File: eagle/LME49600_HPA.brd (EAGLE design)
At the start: 93.7 x 71.1 mm, 43 parts, among them IC1 OPA2134P, IC2 OPA2134P, P1 POLYSWITCH, P2 POLYSWITCH

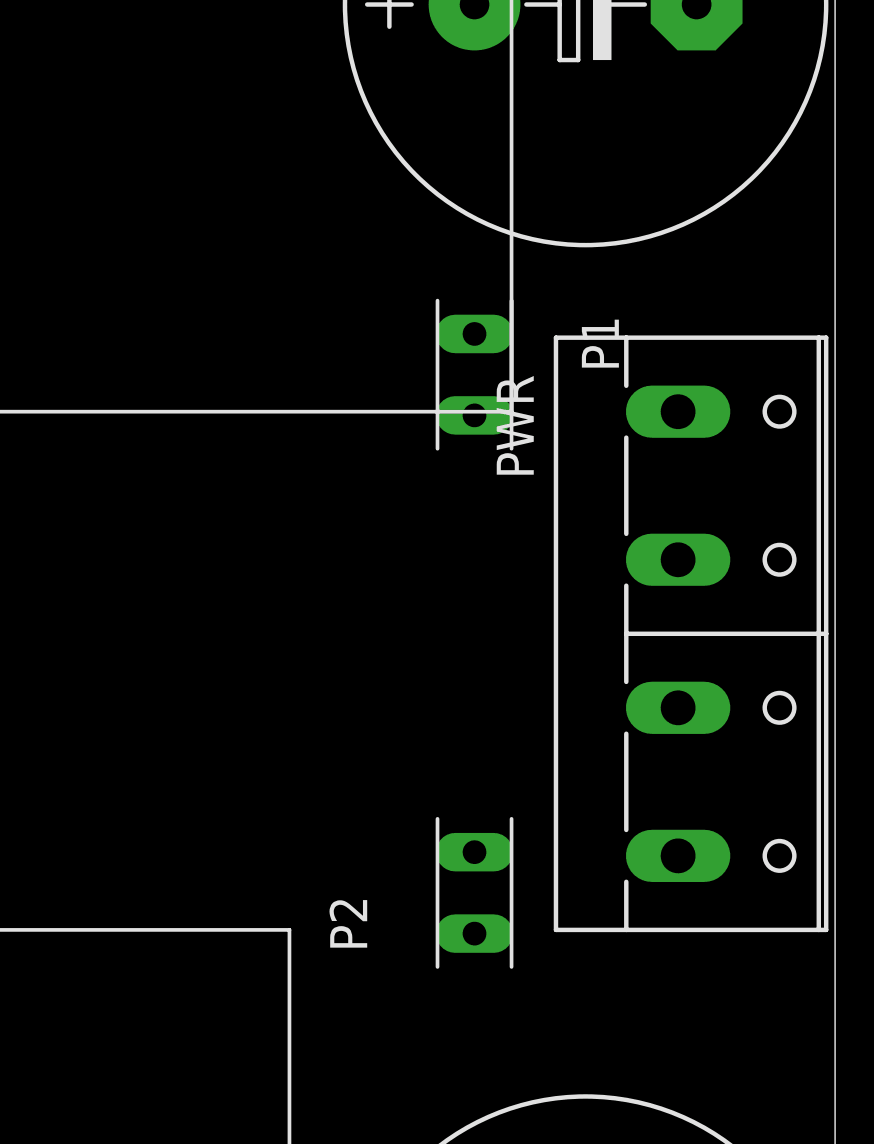
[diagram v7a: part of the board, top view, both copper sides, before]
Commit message: Add: Pilot LED
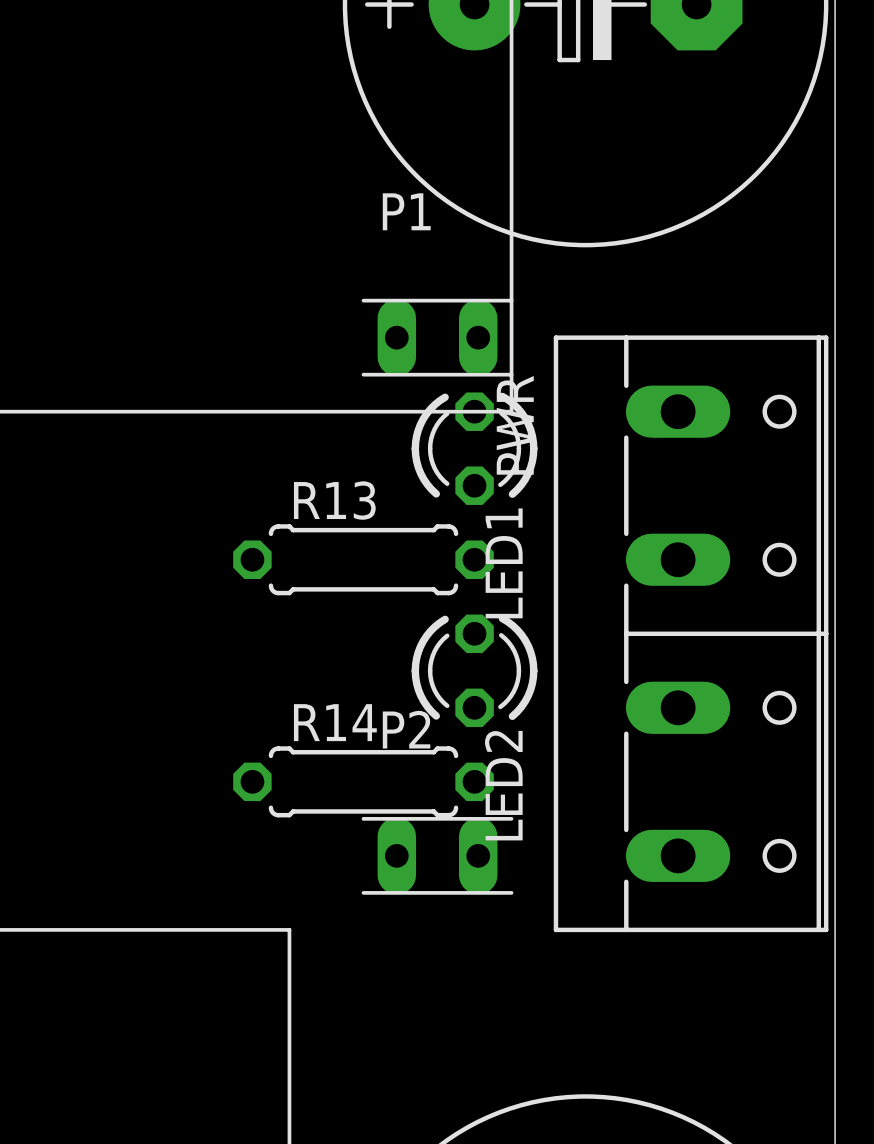
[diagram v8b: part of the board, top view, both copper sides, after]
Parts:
- added LED1: BULE, led:LED3MM
- added LED2: BLUE, led:LED3MM
- added R13, R14: 1k, rcl:0207/7
- moved P2 1.80 mm to (80.0, 30.5), turned to 0 degrees
- moved P1 1.80 mm to (80.0, 48.3), turned to 0 degrees
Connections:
- new net N$17: LED1.K, R13.2
- new net N$19: LED2.K, R14.2
- net AGND: now also LED2.A, R13.1
- net V+: now also LED1.A
- net V-: now also R14.1
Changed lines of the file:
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@@
 <element name="C1" library="rcl" package="E7,5-16" value="470uF" x="85.09" y="59.69"/>
 <element name="C10" library="rcl" package="E7,5-16" value="470uF" x="85.09" y="13.97" rot="R180"/>
-<element name="P1" library="mylib2" package="POLYSWITCH" value="POLYSWITCH" x="81.28" y="46.99" rot="R270"/>
-<element name="P2" library="mylib2" package="POLYSWITCH" value="POLYSWITCH" x="81.28" y="29.21" rot="R90"/>
+<element name="P1" library="mylib2" package="POLYSWITCH" value="POLYSWITCH" x="80.01" y="48.26"/>
+<element name="P2" library="mylib2" package="POLYSWITCH" value="POLYSWITCH" x="80.01" y="30.48"/>
 <element name="C6" library="rcl" package="E2-4" value="4.7uF" x="53.34" y="41.91" rot="R90"/>
 <element name="C7" library="rcl" package="E2-4" value="4.7uF" x="53.34" y="67.31" rot="R270"/>
@@
 <element name="U$1" library="mylib2" package="SIP5-9" value="LME49600-BRD2" x="66.04" y="55.88" rot="R270"/>
 <element name="U$2" library="mylib2" package="SIP5-9" value="LME49600-BRD2" x="58.42" y="17.78" rot="R270"/>
+<element name="LED1" library="led" package="LED3MM" value="BULE" x="81.28" y="44.45" rot="R270"/>
+<element name="LED2" library="led" package="LED3MM" value="BLUE" x="81.28" y="36.83" rot="R270"/>
+<element name="R13" library="rcl" package="0207/7" value="1k" x="77.47" y="40.64"/>
+<element name="R14" library="rcl" package="0207/7" value="1k" x="77.47" y="33.02"/>
 </elements>
 <signals>
@@
 <wire x1="7.62" y1="68.58" x2="35.56" y2="68.58" width="0.4064" layer="16"/>
 <wire x1="5.08" y1="55.88" x2="7.62" y2="53.34" width="0.4064" layer="16"/>
+<contactref element="R13" pad="1"/>
+<contactref element="LED2" pad="A"/>
 <wire x1="88.265" y1="40.64" x2="88.9" y2="59.69" width="0" layer="19" extent="1-1"/>
 <wire x1="88.265" y1="35.56" x2="88.265" y2="40.64" width="0" layer="19" extent="1-1"/>
-<wire x1="88.9" y1="13.97" x2="88.265" y2="35.56" width="0" layer="19" extent="1-1"/>
-<wire x1="53.34" y1="42.926" x2="88.265" y2="40.64" width="0" layer="19" extent="1-1"/>
+<wire x1="81.28" y1="38.1" x2="88.265" y2="40.64" width="0" layer="19" extent="1-1"/>
+<wire x1="73.66" y1="40.64" x2="81.28" y2="38.1" width="0" layer="19" extent="1-1"/>
+<wire x1="53.34" y1="42.926" x2="73.66" y2="40.64" width="0" layer="19" extent="1-1"/>
 <wire x1="43.18" y1="35.56" x2="43.18" y2="38.1" width="0" layer="19" extent="1-1"/>
-<wire x1="45.72" y1="20.574" x2="43.18" y2="35.56" width="0" layer="19" extent="1-1"/>
-<wire x1="35.56" y1="22.86" x2="45.72" y2="20.574" width="0" layer="19" extent="1-1"/>
-<wire x1="35.56" y1="25.4" x2="35.56" y2="22.86" width="0" layer="19" extent="1-1"/>
+<wire x1="35.56" y1="25.4" x2="43.18" y2="35.56" width="0" layer="19" extent="1-1"/>
+<wire x1="35.56" y1="22.86" x2="35.56" y2="25.4" width="0" layer="19" extent="1-1"/>
+<wire x1="45.72" y1="20.574" x2="35.56" y2="22.86" width="0" layer="19" extent="1-1"/>
 <wire x1="45.72" y1="14.986" x2="45.72" y2="20.574" width="0" layer="19" extent="1-1"/>
 <wire x1="53.34" y1="17.78" x2="45.72" y2="20.574" width="0" layer="19" extent="1-1"/>
@@
 <wire x1="17.78" y1="7.62" x2="17.78" y2="15.24" width="0" layer="19" extent="1-1"/>
 <wire x1="25.4" y1="5.08" x2="17.78" y2="7.62" width="0" layer="19" extent="1-1"/>
+<wire x1="88.9" y1="13.97" x2="88.265" y2="35.56" width="0" layer="19" extent="1-1"/>
 </signal>
 <signal name="N$3">
@@
 <wire x1="60.96" y1="60.96" x2="60.96" y2="55.88" width="0.4064" layer="16"/>
 <wire x1="60.96" y1="55.88" x2="58.42" y2="55.88" width="0.4064" layer="16"/>
-<wire x1="81.28" y1="13.97" x2="81.28" y2="27.813" width="0" layer="19" extent="1-1"/>
-<wire x1="53.34" y1="22.86" x2="81.28" y2="27.813" width="0" layer="19" extent="1-1"/>
+<contactref element="R14" pad="1"/>
+<wire x1="73.66" y1="33.02" x2="78.613" y2="30.48" width="0" layer="19" extent="1-1"/>
+<wire x1="81.28" y1="13.97" x2="78.613" y2="30.48" width="0" layer="19" extent="1-1"/>
+<wire x1="53.34" y1="22.86" x2="73.66" y2="33.02" width="0" layer="19" extent="1-1"/>
 <wire x1="50.8" y1="22.86" x2="53.34" y2="22.86" width="0" layer="19" extent="1-1"/>
 <wire x1="50.8" y1="17.78" x2="50.8" y2="22.86" width="0" layer="19" extent="1-1"/>
@@
 <wire x1="22.86" y1="22.86" x2="45.72" y2="22.606" width="0" layer="19" extent="1-1"/>
 <wire x1="17.78" y1="22.86" x2="22.86" y2="22.86" width="0" layer="19" extent="1-1"/>
-<wire x1="58.42" y1="55.88" x2="53.34" y2="22.86" width="0" layer="19" extent="1-1"/>
+<wire x1="60.96" y1="55.88" x2="73.66" y2="33.02" width="0" layer="19" extent="16-16"/>
 </signal>
 <signal name="V+">
@@
 <wire x1="52.07" y1="48.26" x2="55.88" y2="48.26" width="0.4064" layer="16"/>
 <wire x1="55.88" y1="48.26" x2="58.42" y2="50.8" width="0.4064" layer="16"/>
-<wire x1="81.28" y1="48.387" x2="81.28" y2="59.69" width="0" layer="19" extent="1-1"/>
-<wire x1="58.42" y1="50.8" x2="81.28" y2="48.387" width="0" layer="19" extent="1-1"/>
+<contactref element="LED1" pad="A"/>
+<wire x1="78.613" y1="48.26" x2="81.28" y2="59.69" width="0" layer="19" extent="1-1"/>
+<wire x1="81.28" y1="45.72" x2="78.613" y2="48.26" width="0" layer="19" extent="1-1"/>
+<wire x1="58.42" y1="50.8" x2="78.613" y2="48.26" width="0" layer="19" extent="1-1"/>
 <wire x1="53.34" y1="40.894" x2="52.07" y2="48.26" width="0" layer="19" extent="16-16"/>
 <wire x1="53.34" y1="12.7" x2="53.34" y2="40.894" width="0" layer="19" extent="1-1"/>
@@
 <contactref element="P1" pad="2"/>
 <contactref element="PWR" pad="1"/>
-<wire x1="81.28" y1="45.593" x2="88.265" y2="45.72" width="0" layer="19" extent="1-1"/>
+<wire x1="81.407" y1="48.26" x2="88.265" y2="45.72" width="0" layer="19" extent="1-1"/>
 </signal>
 <signal name="PW-">
 <contactref element="P2" pad="2"/>
 <contactref element="PWR" pad="4"/>
-<wire x1="81.28" y1="30.607" x2="88.265" y2="30.48" width="0" layer="19" extent="1-1"/>
+<wire x1="81.407" y1="30.48" x2="88.265" y2="30.48" width="0" layer="19" extent="1-1"/>
 </signal>
 <signal name="N$1">
@@
 <wire x1="17.78" y1="33.02" x2="25.4" y2="27.94" width="0" layer="19" extent="1-1"/>
 </signal>
+<signal name="N$17">
+<contactref element="R13" pad="2"/>
+<contactref element="LED1" pad="K"/>
+<wire x1="81.28" y1="40.64" x2="81.28" y2="43.18" width="0" layer="19" extent="1-1"/>
+</signal>
+<signal name="N$19">
+<contactref element="R14" pad="2"/>
+<contactref element="LED2" pad="K"/>
+<wire x1="81.28" y1="33.02" x2="81.28" y2="35.56" width="0" layer="19" extent="1-1"/>
+</signal>
 </signals>
